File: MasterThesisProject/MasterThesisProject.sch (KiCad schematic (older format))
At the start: 44 parts

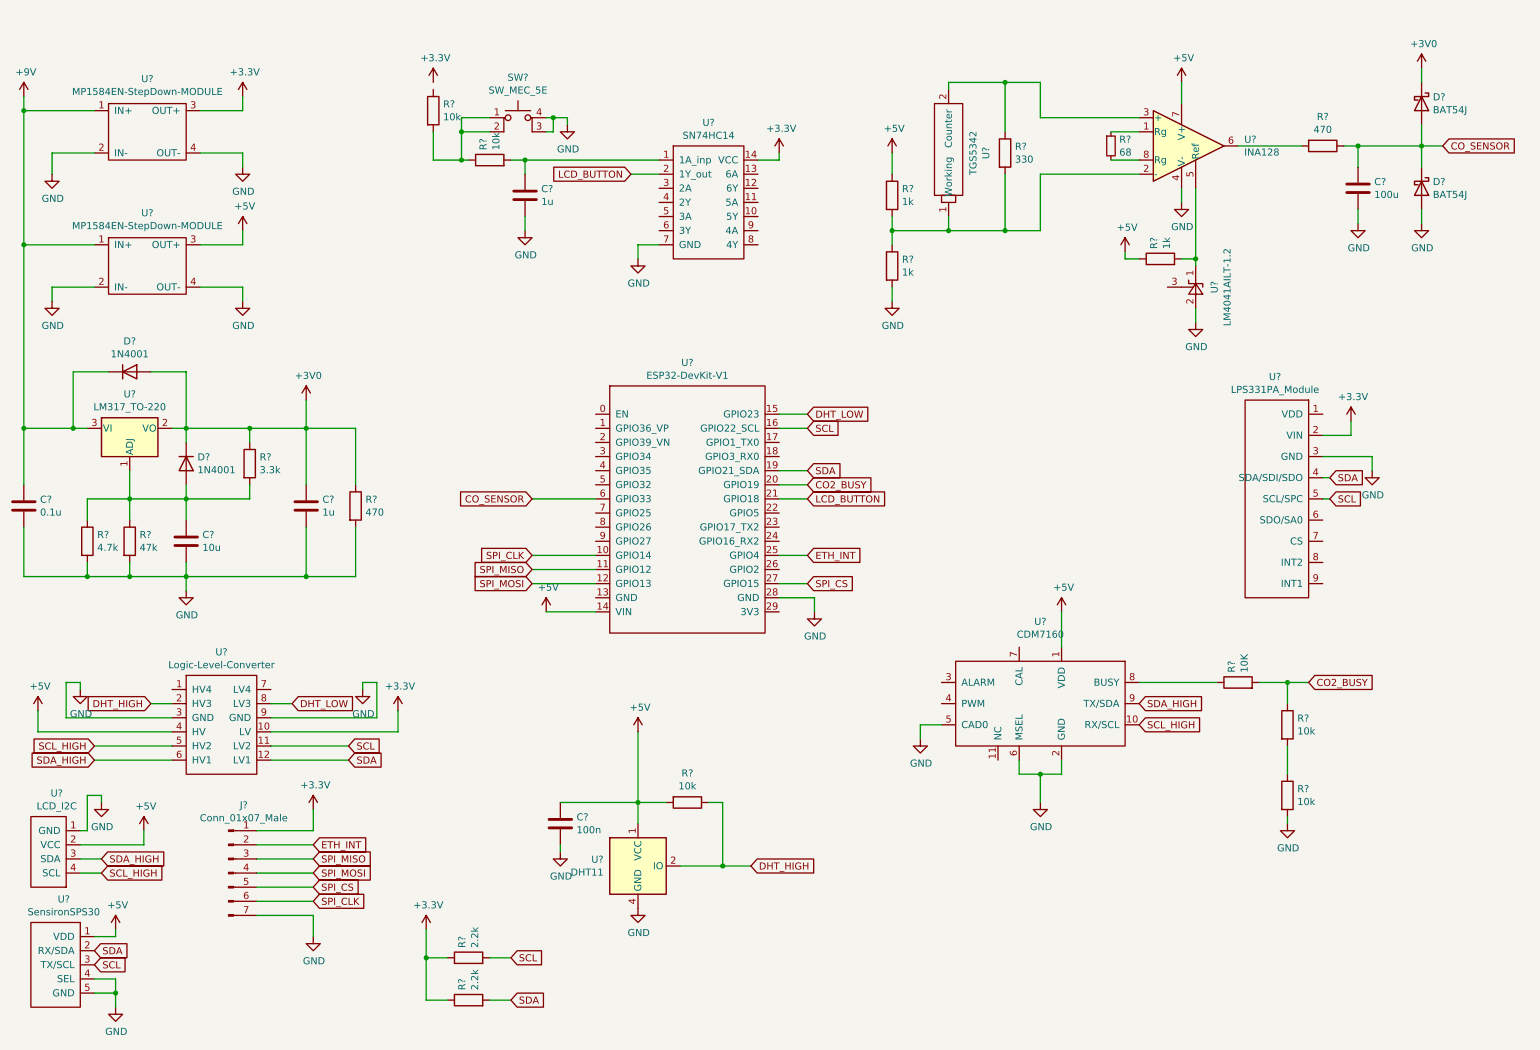
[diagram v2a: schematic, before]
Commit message: Add footprints to all elements
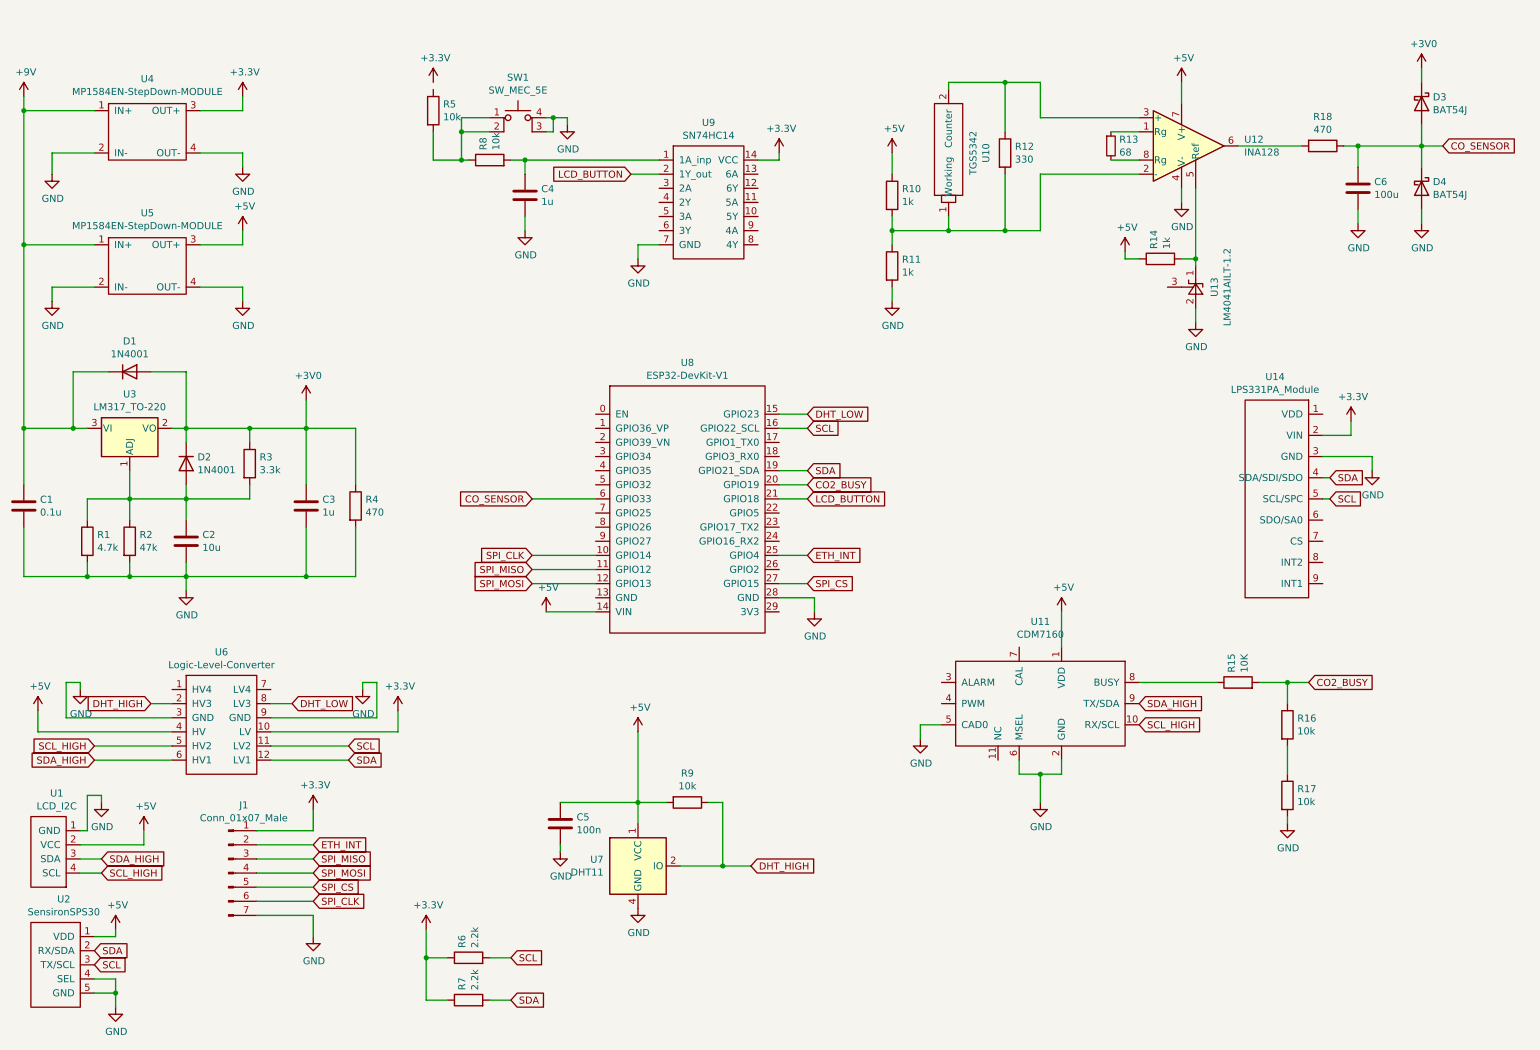
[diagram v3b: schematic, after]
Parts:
- C1, C2, C3, C4, C5, C6: renamed from C?; footprint (none) -> Capacitor_SMD:C_0805_2012Metric_Pad1.18x1.45mm_HandSolder
- J1: renamed from J?; footprint (none) -> Connector_PinHeader_2.54mm:PinHeader_1x07_P2.54mm_Vertical
- SW1: renamed from SW?; footprint (none) -> Connector_PinSocket_2.54mm:PinSocket_1x04_P2.54mm_Vertical
- U1, U2: renamed from U?; footprint (none) -> Connector_PinHeader_2.54mm:PinHeader_1x04_P2.54mm_Vertical
- U10: renamed from U?; footprint (none) -> CustomFootprints:TGS_5342
- U11: renamed from U?; footprint (none) -> CustomFootprints:CDM7160
- U12: renamed from U?; footprint (none) -> Package_SO:SOIC-8_3.9x4.9mm_P1.27mm
- U13: renamed from U?; footprint Package_SOT23 -> Package_TO_SOT_SMD:SOT-23
- U14: renamed from U?; footprint (none) -> CustomFootprints:LPS331AP_Module
- U8: renamed from U?; footprint (none) -> CustomFootprints:ESP_DEVKIT_V1_30_PIN
- U9: renamed from U?; footprint (none) -> Package_DIP:DIP-14_W7.62mm
- gave numbers to parts that had none: 27

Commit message: Add init version of components locations
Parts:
- U2: footprint Connector_PinHeader_2.54mm:PinHeader_1x04_P2.54mm_Vertical -> Connector_PinHeader_2.54mm:PinHeader_1x05_P2.54mm_Vertical
- U4, U5: footprint (none) -> CustomFootprints:MP2307_module
- U6: footprint (none) -> CustomFootprints:Logic-Level-Converter
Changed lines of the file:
@@
 F 0 "U6" H 2050 6015 50  0000 C CNN
 F 1 "Logic-Level-Converter" H 2050 5924 50  0000 C CNN
-F 2 "" H 2050 5000 50  0001 C CNN
+F 2 "CustomFootprints:Logic-Level-Converter" H 2050 5000 50  0001 C CNN
 F 3 "" H 2050 5000 50  0001 C CNN
 	1    2050 5500
@@
 F 0 "U4" H 1525 1975 50  0000 C CNN
 F 1 "MP1584EN-StepDown-MODULE" H 1525 1884 50  0000 C CNN
-F 2 "" H 1500 1200 50  0001 C CNN
+F 2 "CustomFootprints:MP2307_module" H 1500 1200 50  0001 C CNN
 F 3 "" H 1500 1200 50  0001 C CNN
 	1    1500 1450
@@
 F 0 "U5" H 1525 2925 50  0000 C CNN
 F 1 "MP1584EN-StepDown-MODULE" H 1525 2834 50  0000 C CNN
-F 2 "" H 1500 2150 50  0001 C CNN
+F 2 "CustomFootprints:MP2307_module" H 1500 2150 50  0001 C CNN
 F 3 "" H 1500 2150 50  0001 C CNN
 	1    1500 2400
@@
 F 0 "U2" H 933 8365 50  0000 C CNN
 F 1 "SensironSPS30" H 933 8274 50  0000 C CNN
-F 2 "Connector_PinHeader_2.54mm:PinHeader_1x04_P2.54mm_Vertical" H 900 7550 50  0001 C CNN
+F 2 "Connector_PinHeader_2.54mm:PinHeader_1x05_P2.54mm_Vertical" H 900 7550 50  0001 C CNN
 F 3 "" H 900 7550 50  0001 C CNN
 	1    900  7550

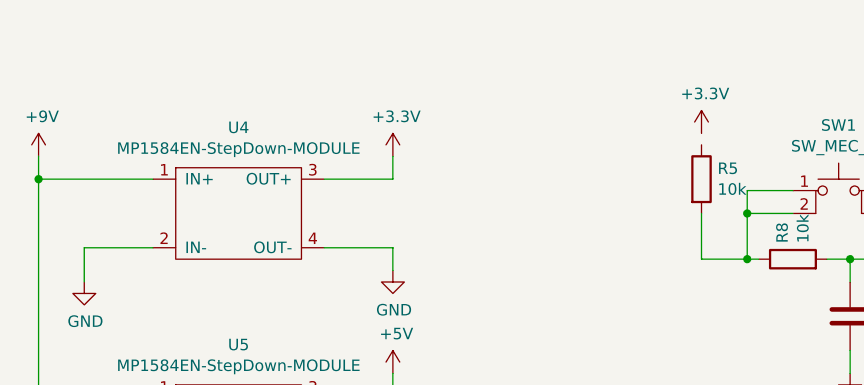
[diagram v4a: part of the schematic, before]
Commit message: Connect all elements to GND, minor updates to schematic
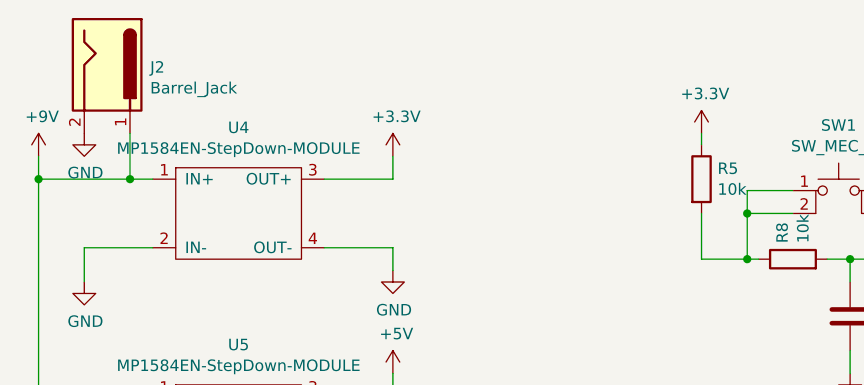
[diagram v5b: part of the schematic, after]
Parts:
- added J2: Barrel_Jack, Connector_BarrelJack:BarrelJack_Horizontal, symbol Connector:Barrel_Jack
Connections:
- net +3V3: now also R5.1
- net +9V: now also J2.1
- net GND: now also J2.2
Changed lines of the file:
@@
 	850  1450 1150 1450
 Wire Wire Line
-	650  1150 1150 1150
+	650  1150 1050 1150
 Wire Wire Line
 	650  2100 1150 2100
@@
 Wire Wire Line
 	9600 5650 9600 5850
+Wire Wire Line
+	3550 1000 3550 950
+Wire Wire Line
+	1050 950  1050 1150
+Connection ~ 1050 1150
+Wire Wire Line
+	1050 1150 1150 1150
+$Comp
+L power:GND #PWR046
+U 1 1 607FD3F5
+P 850 950
+F 0 "#PWR046" H 850 700 50  0001 C CNN
+F 1 "GND" H 855 777 50  0000 C CNN
+F 2 "" H 850 950 50  0001 C CNN
+F 3 "" H 850 950 50  0001 C CNN
+	1    850  950
+	1    0    0    -1
+$EndComp
+$Comp
+L Connector:Barrel_Jack J2
+U 1 1 6080CABE
+P 950 650
+F 0 "J2" V 961 838 50  0000 L CNN
+F 1 "Barrel_Jack" V 1052 838 50  0000 L CNN
+F 2 "Connector_BarrelJack:BarrelJack_Horizontal" H 1000 610 50  0001 C CNN
+F 3 "~" H 1000 610 50  0001 C CNN
+	1    950  650
+	0    1    1    0
+$EndComp
 $EndSCHEMATC

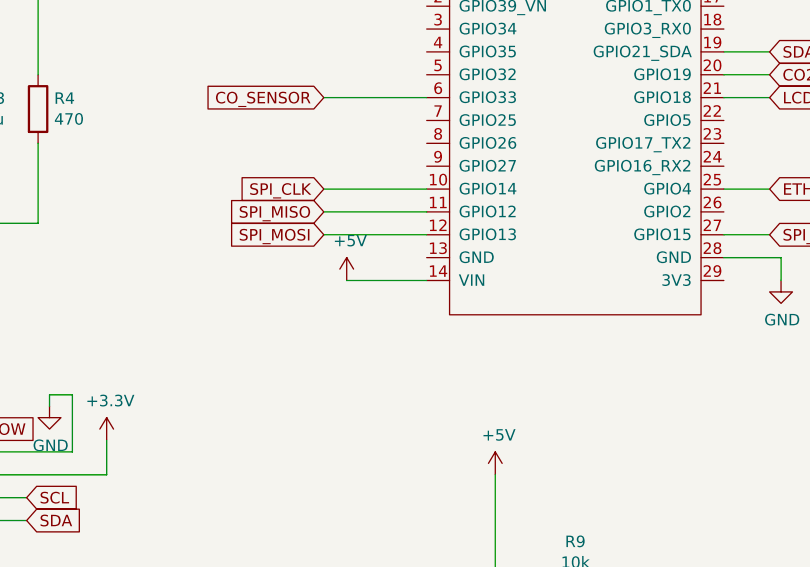
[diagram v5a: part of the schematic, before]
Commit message: Add all missing connections to pcb
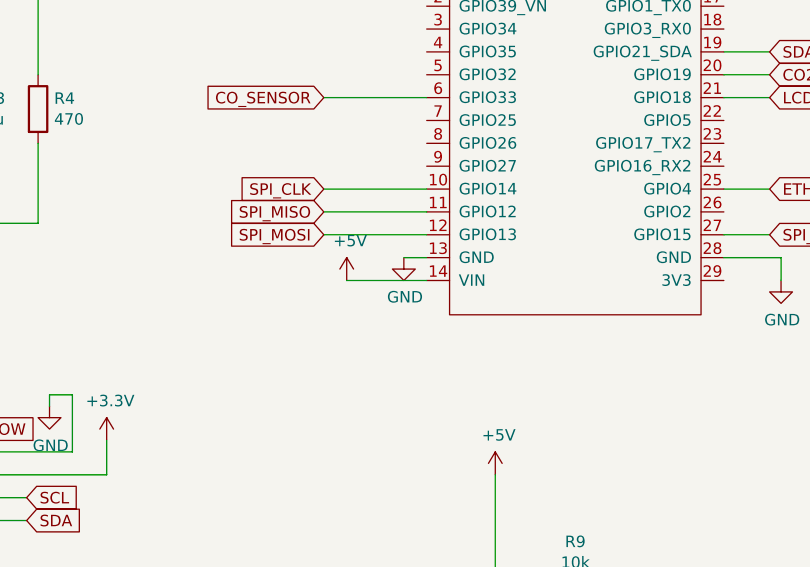
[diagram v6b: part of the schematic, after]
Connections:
- net GND: now also U8.13 (GND)
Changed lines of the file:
@@
 	0    1    1    0
 $EndComp
+$Comp
+L power:GND #PWR?
+U 1 1 607EA17B
+P 4600 4600
+F 0 "#PWR?" H 4600 4350 50  0001 C CNN
+F 1 "GND" H 4605 4427 50  0000 C CNN
+F 2 "" H 4600 4600 50  0001 C CNN
+F 3 "" H 4600 4600 50  0001 C CNN
+	1    4600 4600
+	1    0    0    -1
+$EndComp
+Wire Wire Line
+	4700 4600 4600 4600
 $EndSCHEMATC

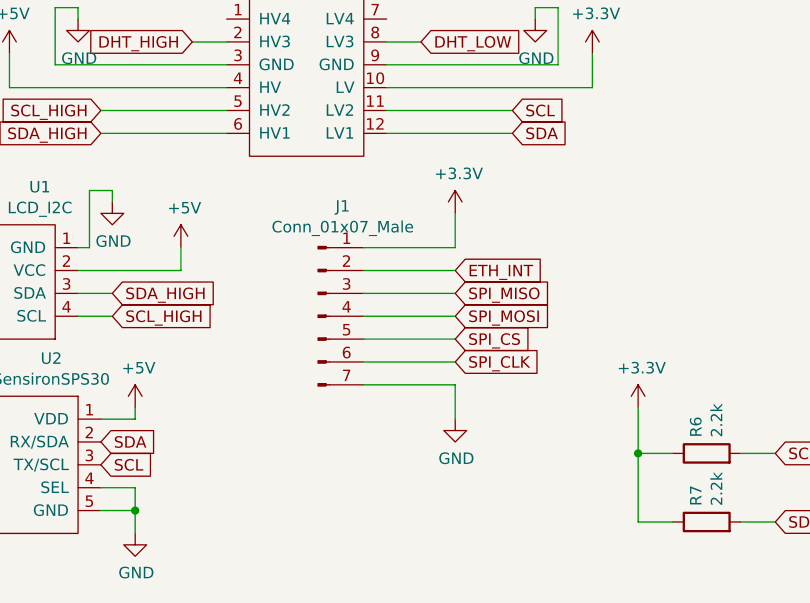
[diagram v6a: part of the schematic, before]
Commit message: Update W5500 schematic and PCB to match custom PCB connectino
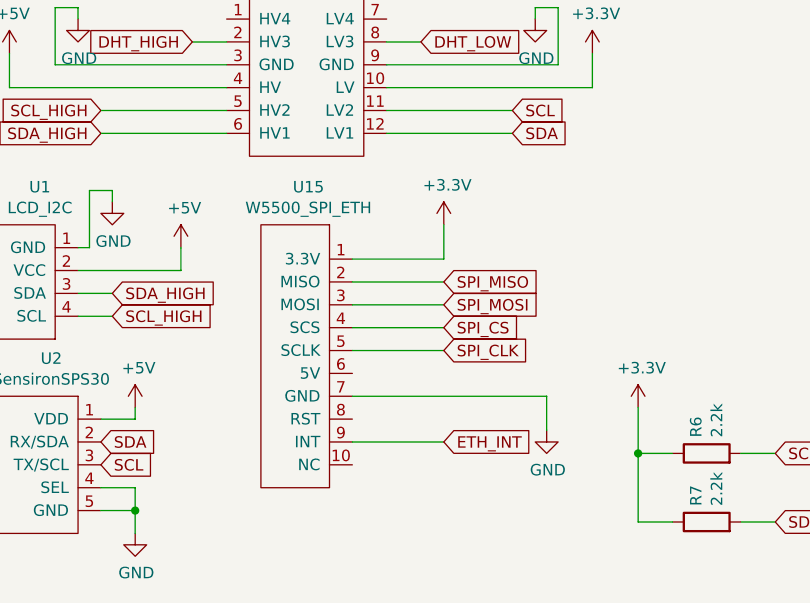
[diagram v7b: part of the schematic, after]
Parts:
- removed J1: Conn_01x07_Male, Connector_PinHeader_2.54mm:PinHeader_1x07_P2.54mm_Vertical, symbol Connector:Conn_01x07_Male
- added U15: W5500_SPI_ETH, CustomFootprints:W5500_SPI_ETH, symbol AirControl:W5500_SPI_ETH
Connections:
- net +3V3: now also U15.1 (3.3V)
- net ETH_INT: now also U15.9 (INT)
- net GND: now also U15.7 (GND)
- net SPI_CLK: now also U15.5 (SCLK)
- net SPI_CS: now also U15.4 (SCS)
- net SPI_MISO: now also U15.2 (MISO)
- net SPI_MOSI: now also U15.3 (MOSI)
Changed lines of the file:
@@
 Wire Wire Line
 	1800 4550 1800 4450
-$Comp
-L Connector:Conn_01x07_Male J1
-U 1 1 608ED61E
-P 2100 6550
-F 0 "J1" H 2208 7031 50  0000 C CNN
-F 1 "Conn_01x07_Male" H 2208 6940 50  0000 C CNN
-F 2 "Connector_PinHeader_2.54mm:PinHeader_1x07_P2.54mm_Vertical" H 2100 6550 50  0001 C CNN
-F 3 "~" H 2100 6550 50  0001 C CNN
-	1    2100 6550
-	1    0    0    -1
-$EndComp
 Text GLabel 4250 4500 0    50   Input ~ 0
 SPI_MOSI
@@
 	6200 4300 6000 4300
 Wire Wire Line
-	2300 6250 2700 6250
+	2250 6300 2650 6300
 Wire Wire Line
-	2700 6250 2700 6100
-Wire Wire Line
-	2300 6850 2700 6850
-Wire Wire Line
-	2700 6850 2700 7000
+	2650 6300 2650 6150
 $Comp
 L power:GND #PWR017
 U 1 1 6095011A
-P 2700 7000
-F 0 "#PWR017" H 2700 6750 50  0001 C CNN
-F 1 "GND" H 2705 6827 50  0000 C CNN
-F 2 "" H 2700 7000 50  0001 C CNN
-F 3 "" H 2700 7000 50  0001 C CNN
-	1    2700 7000
+P 3100 7050
+F 0 "#PWR017" H 3100 6800 50  0001 C CNN
+F 1 "GND" H 3105 6877 50  0000 C CNN
+F 2 "" H 3100 7050 50  0001 C CNN
+F 3 "" H 3100 7050 50  0001 C CNN
+	1    3100 7050
 	1    0    0    -1
 $EndComp
@@
 L power:+3.3V #PWR016
 U 1 1 60950EB2
-P 2700 6100
-F 0 "#PWR016" H 2700 5950 50  0001 C CNN
-F 1 "+3.3V" H 2715 6273 50  0000 C CNN
-F 2 "" H 2700 6100 50  0001 C CNN
-F 3 "" H 2700 6100 50  0001 C CNN
-	1    2700 6100
+P 2650 6150
+F 0 "#PWR016" H 2650 6000 50  0001 C CNN
+F 1 "+3.3V" H 2665 6323 50  0000 C CNN
+F 2 "" H 2650 6150 50  0001 C CNN
+F 3 "" H 2650 6150 50  0001 C CNN
+	1    2650 6150
 	1    0    0    -1
 $EndComp
-Text GLabel 2700 6350 2    50   Input ~ 0
+Text GLabel 2650 7100 2    50   Input ~ 0
 ETH_INT
-Text GLabel 2700 6450 2    50   Input ~ 0
+Text GLabel 2650 6400 2    50   Input ~ 0
 SPI_MISO
-Text GLabel 2700 6550 2    50   Input ~ 0
+Text GLabel 2650 6500 2    50   Input ~ 0
 SPI_MOSI
-Text GLabel 2700 6650 2    50   Input ~ 0
+Text GLabel 2650 6600 2    50   Input ~ 0
 SPI_CS
-Text GLabel 2700 6750 2    50   Input ~ 0
+Text GLabel 2650 6700 2    50   Input ~ 0
 SPI_CLK
 Wire Wire Line
-	2700 6350 2300 6350
+	2650 7100 2250 7100
 Wire Wire Line
-	2300 6450 2700 6450
+	2250 6400 2650 6400
 Wire Wire Line
-	2700 6550 2300 6550
+	2650 6500 2250 6500
 Wire Wire Line
-	2300 6650 2700 6650
+	2250 6600 2650 6600
 Wire Wire Line
-	2700 6750 2300 6750
+	2650 6700 2250 6700
 Wire Wire Line
 	4700 3900 4250 3900
@@
 $EndComp
 $Comp
-L power:GND #PWR?
+L power:GND #PWR047
 U 1 1 607EA17B
 P 4600 4600
-F 0 "#PWR?" H 4600 4350 50  0001 C CNN
+F 0 "#PWR047" H 4600 4350 50  0001 C CNN
 F 1 "GND" H 4605 4427 50  0000 C CNN
 F 2 "" H 4600 4600 50  0001 C CNN
@@
 Wire Wire Line
 	4700 4600 4600 4600
+$Comp
+L AirControl:W5500_SPI_ETH U15
+U 1 1 6086F670
+P 2000 7450
+F 0 "U15" H 2058 8915 50  0000 C CNN
+F 1 "W5500_SPI_ETH" H 2058 8824 50  0000 C CNN
+F 2 "CustomFootprints:W5500_SPI_ETH" H 2000 7450 50  0001 C CNN
+F 3 "" H 2000 7450 50  0001 C CNN
+	1    2000 7450
+	1    0    0    -1
+$EndComp
+Wire Wire Line
+	3100 6900 3100 7050
+Wire Wire Line
+	2250 6900 3100 6900
 $EndSCHEMATC

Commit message: Remove old pcb, port elements to new one
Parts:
- J2: footprint Connector_BarrelJack:BarrelJack_Horizontal -> Connector_PinSocket_2.54mm:PinSocket_1x02_P2.54mm_Vertical
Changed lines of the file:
@@
 F 0 "J2" V 961 838 50  0000 L CNN
 F 1 "Barrel_Jack" V 1052 838 50  0000 L CNN
-F 2 "Connector_BarrelJack:BarrelJack_Horizontal" H 1000 610 50  0001 C CNN
+F 2 "Connector_PinSocket_2.54mm:PinSocket_1x02_P2.54mm_Vertical" H 1000 610 50  0001 C CNN
 F 3 "~" H 1000 610 50  0001 C CNN
 	1    950  650
